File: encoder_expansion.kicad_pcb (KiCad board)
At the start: 2 copper layers, 33 x 62.2 mm, 7 parts, among them J1 Conn_01x05_Socket, J2 Conn_01x05_Socket, J3 Conn_01x04_Socket, J4 Conn_01x04_Socket, J5 Conn_01x04_Socket, J6 Conn_01x04_Socket, J7 Conn_01x02_Socket

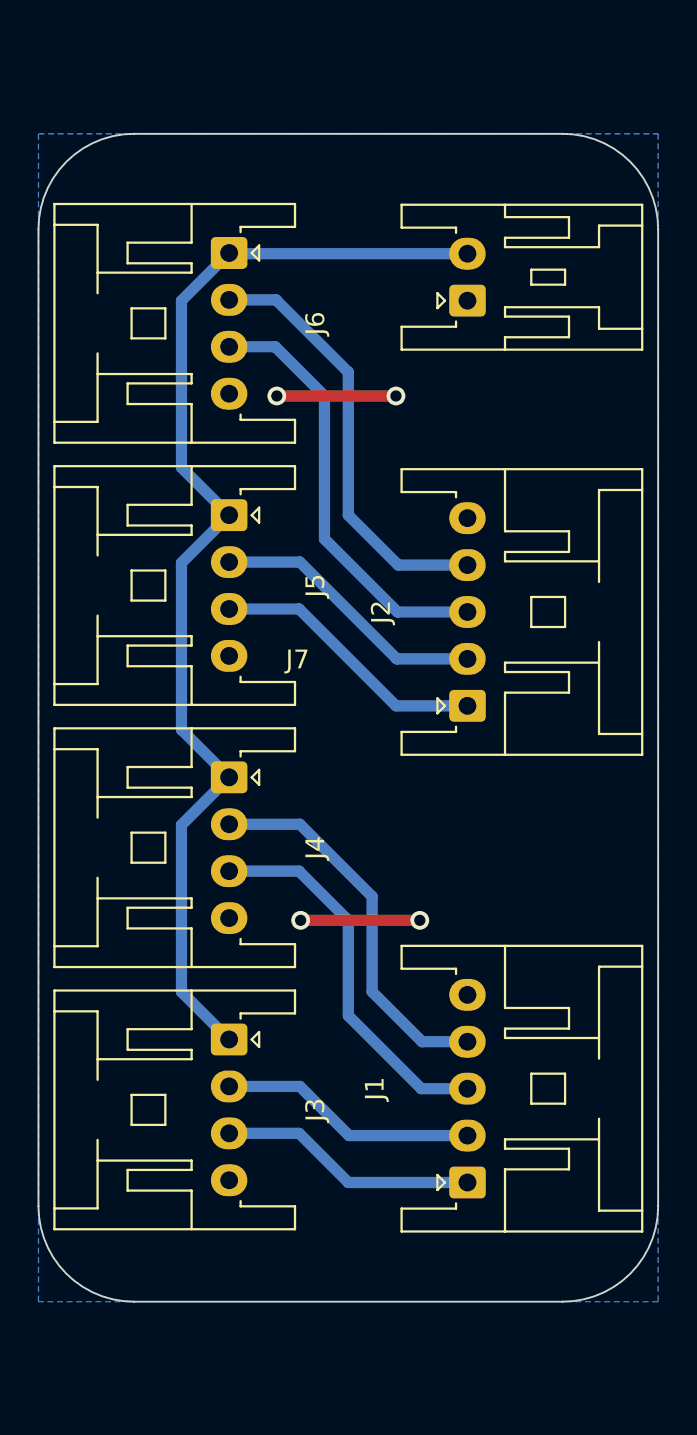
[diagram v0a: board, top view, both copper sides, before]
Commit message: add mounting hole and silk
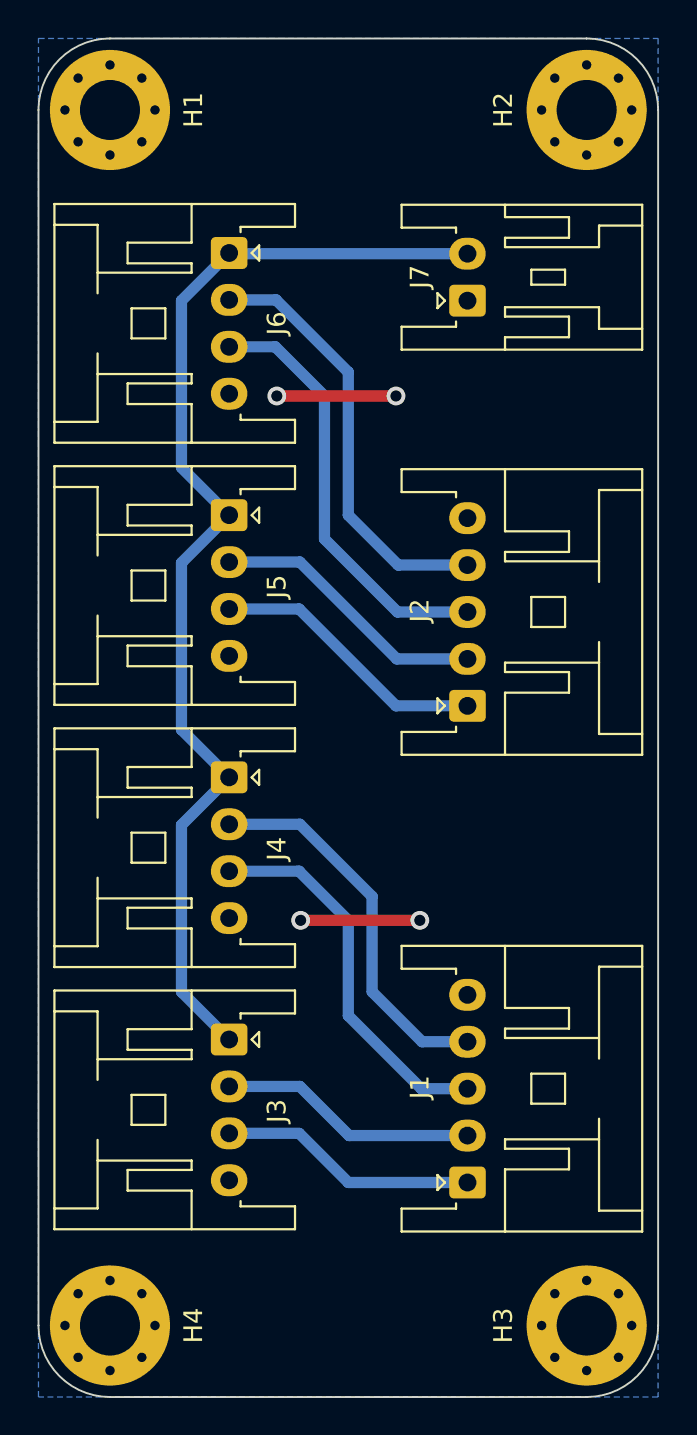
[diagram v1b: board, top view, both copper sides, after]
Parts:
- added H1: MountingHole, MountingHole:MountingHole_3.2mm_M3_Pad_Via, F.Cu at (121.9, 69.8)
- added H2: MountingHole, MountingHole:MountingHole_3.2mm_M3_Pad_Via, F.Cu at (147.3, 69.8)
- added H3: MountingHole, MountingHole:MountingHole_3.2mm_M3_Pad_Via, F.Cu at (147.3, 134.6)
- added H4: MountingHole, MountingHole:MountingHole_3.2mm_M3_Pad_Via, F.Cu at (121.9, 134.6)
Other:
- board size 33 x 62.2 mm -> 33 x 72.4 mm
- board text added: "A:PC11 B:PC10"
- board text added: "A:PC5 B:PC4"
- board text added: "A:PC7 B:PC6"
- board text added: "A:PC9 B:PC8"
- board text added: "github.com/paripalpp/ RPHAT_nucleo_expand_encoder"
